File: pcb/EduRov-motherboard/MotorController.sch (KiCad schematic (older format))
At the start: 10 parts, among them IC401 L6203, U201 ACS723xLCTR-05AB

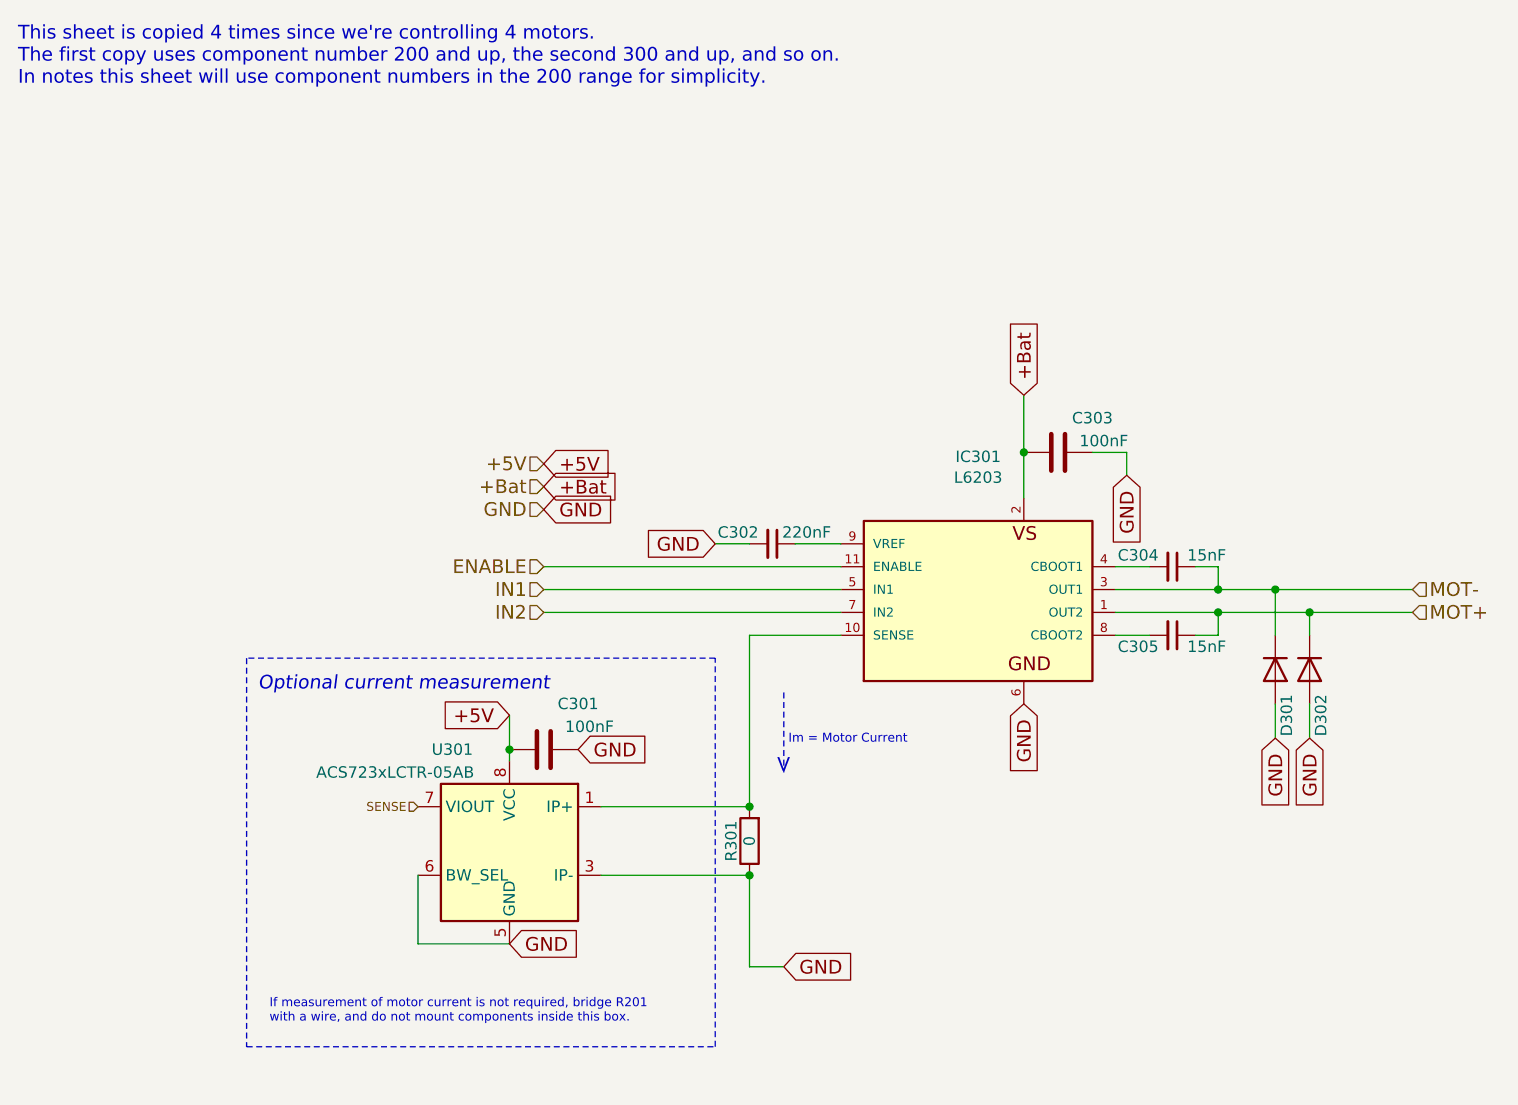
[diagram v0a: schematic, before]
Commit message: Update footprints with models
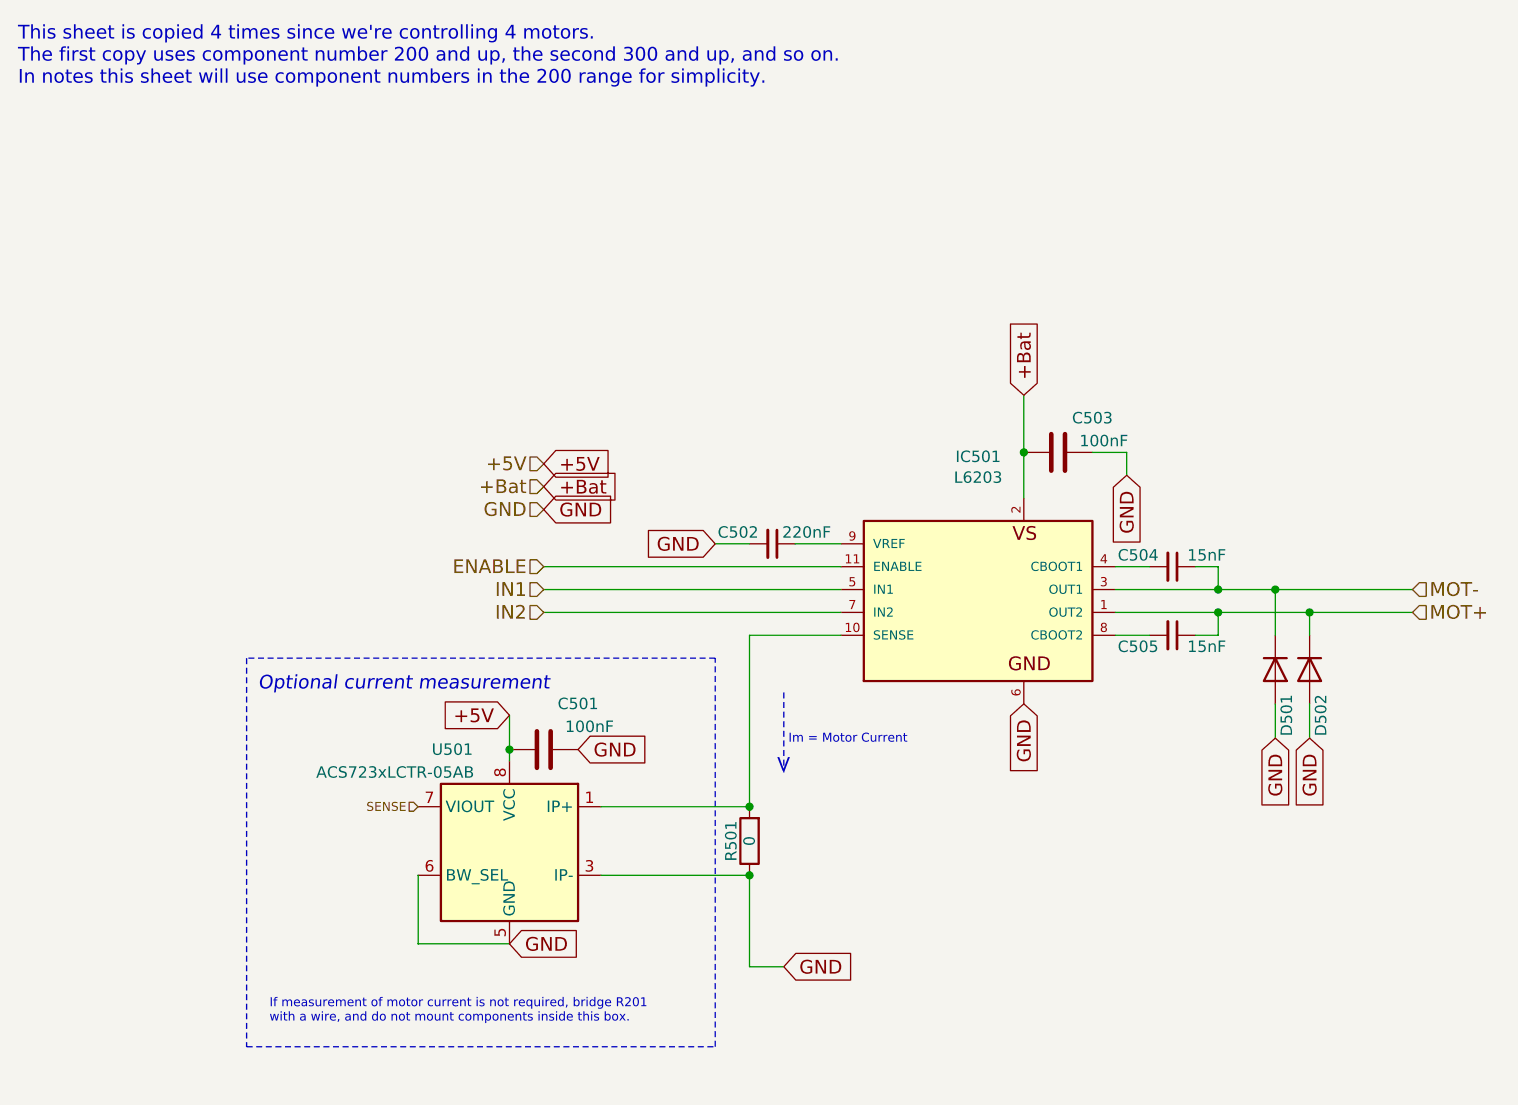
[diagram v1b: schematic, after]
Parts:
- IC401: footprint SnapEDA Library:MULTIWATT-11 -> EduRov:MULTIWATT-11
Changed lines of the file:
@@
 $Descr A4 11693 8268
 encoding utf-8
-Sheet 3 5
+Sheet 5 5
 Title ""
 Date ""
@@
 AR Path="/6003F027/5FFEEEFF" Ref="D402"  Part="1"
 AR Path="/60043462/5FFEEEFF" Ref="D502"  Part="1"
-F 0 "D302" H 6450 3500 50  0000 C CNN
+F 0 "D502" H 6450 3500 50  0000 C CNN
 F 1 "D" H 6400 3400 50  0001 C CNN
 F 2 "Diode_THT:D_DO-41_SOD81_P3.81mm_Vertical_KathodeUp" H 6250 3450 50  0001 C CNN
@@
 AR Path="/6003F027/5FFEEF0B" Ref="D401"  Part="1"
 AR Path="/60043462/5FFEEF0B" Ref="D501"  Part="1"
-F 0 "D301" H 6300 3500 50  0000 C CNN
+F 0 "D501" H 6300 3500 50  0000 C CNN
 F 1 "D" H 6250 3400 50  0001 C CNN
 F 2 "Diode_THT:D_DO-41_SOD81_P3.81mm_Vertical_KathodeUp" H 6100 3450 50  0001 C CNN
@@
 AR Path="/6003F027/5FFEEF49" Ref="C404"  Part="1"
 AR Path="/60043462/5FFEEF49" Ref="C504"  Part="1"
-F 0 "C304" V 5600 2850 50  0000 C CNN
+F 0 "C504" V 5600 2850 50  0000 C CNN
 F 1 "15nF" V 5600 3150 50  0000 C CNN
 F 2 "Capacitor_THT:C_Disc_D3.8mm_W2.6mm_P2.50mm" H 5650 3000 50  0001 C CNN
@@
 AR Path="/6003F027/5FFEEF54" Ref="C405"  Part="1"
 AR Path="/60043462/5FFEEF54" Ref="C505"  Part="1"
-F 0 "C305" V 5700 3150 50  0000 C CNN
+F 0 "C505" V 5700 3150 50  0000 C CNN
 F 1 "15nF" V 5700 3450 50  0000 C CNN
 F 2 "Capacitor_THT:C_Disc_D3.8mm_W2.6mm_P2.50mm" H 5650 3300 50  0001 C CNN
@@
 AR Path="/6003F027/5FFEEF6B" Ref="C402"  Part="1"
 AR Path="/60043462/5FFEEF6B" Ref="C502"  Part="1"
-F 0 "C302" V 3850 2750 50  0000 C CNN
+F 0 "C502" V 3850 2750 50  0000 C CNN
 F 1 "220nF" V 3850 3050 50  0000 C CNN
 F 2 "Capacitor_THT:C_Disc_D3.8mm_W2.6mm_P2.50mm" H 3900 2900 50  0001 C CNN
@@
 AR Path="/6003A868/600F7A3C" Ref="C303"  Part="1"
 AR Path="/6003F027/600F7A3C" Ref="C403"  Part="1"
-F 0 "C303" V 5300 2650 50  0000 C CNN
+F 0 "C503" V 5300 2650 50  0000 C CNN
 F 1 "100nF" V 5200 2700 50  0000 C CNN
 F 2 "Capacitor_THT:C_Disc_D5.0mm_W2.5mm_P2.50mm" H 5188 2350 50  0001 C CNN
@@
 AR Path="/6003F027/6032BA93" Ref="R401"  Part="1"
 AR Path="/60043462/6032BA93" Ref="R501"  Part="1"
-F 0 "R301" V 3880 4200 50  0000 C CNN
+F 0 "R501" V 3880 4200 50  0000 C CNN
 F 1 "0" V 3800 4200 50  0000 C CNN
 F 2 "Resistor_THT:R_Axial_DIN0204_L3.6mm_D1.6mm_P1.90mm_Vertical" V 3730 4200 50  0001 C CNN
@@
 AR Path="/6003F027/60485F83" Ref="U401"  Part="1"
 AR Path="/60043462/60485F83" Ref="U501"  Part="1"
-F 0 "U301" H 3000 4700 50  0000 C CNN
+F 0 "U501" H 3000 4700 50  0000 C CNN
 F 1 "ACS723xLCTR-05AB" H 3250 4600 50  0000 C CNN
 F 2 "Package_SO:SOIC-8_3.9x4.9mm_P1.27mm" H 2850 3900 50  0001 L CIN
@@
 AR Path="/6003A868/60487676" Ref="C301"  Part="1"
 AR Path="/6003F027/60487676" Ref="C401"  Part="1"
-F 0 "C301" V 3100 3950 50  0000 C CNN
+F 0 "C501" V 3100 3950 50  0000 C CNN
 F 1 "100nF" V 3000 4000 50  0000 C CNN
 F 2 "Capacitor_THT:C_Disc_D5.0mm_W2.5mm_P2.50mm" H 2938 3650 50  0001 C CNN
@@
 AR Path="/6003A868/60738BFF" Ref="IC301"  Part="1"
 AR Path="/60043462/60738BFF" Ref="IC501"  Part="1"
-F 0 "IC301" H 4800 3681 50  0000 C CNN
+F 0 "IC501" H 4800 3681 50  0000 C CNN
 F 1 "L6203" H 4800 3590 50  0000 C CNN
-F 2 "SnapEDA Library:MULTIWATT-11" H 4800 3100 50  0001 L BNN
+F 2 "EduRov:MULTIWATT-11" H 4800 3100 50  0001 L BNN
 F 3 "" H 4800 3100 50  0001 L BNN
 F 4 "" H 4800 3100 50  0001 L BNN "MF"

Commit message: Update BOM
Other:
- note added: "If the allegro part is hard to find, \nTMCS1101A4BQDR is a drop-in replacement."
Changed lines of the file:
@@
 $Descr A4 11693 8268
 encoding utf-8
-Sheet 5 5
+Sheet 2 5
 Title ""
 Date ""
@@
 AR Path="/6003F027/5FFEEEFF" Ref="D402"  Part="1"
 AR Path="/60043462/5FFEEEFF" Ref="D502"  Part="1"
-F 0 "D502" H 6450 3500 50  0000 C CNN
+F 0 "D202" H 6450 3500 50  0000 C CNN
 F 1 "D" H 6400 3400 50  0001 C CNN
 F 2 "Diode_THT:D_DO-41_SOD81_P3.81mm_Vertical_KathodeUp" H 6250 3450 50  0001 C CNN
@@
 AR Path="/6003F027/5FFEEF0B" Ref="D401"  Part="1"
 AR Path="/60043462/5FFEEF0B" Ref="D501"  Part="1"
-F 0 "D501" H 6300 3500 50  0000 C CNN
+F 0 "D201" H 6300 3500 50  0000 C CNN
 F 1 "D" H 6250 3400 50  0001 C CNN
 F 2 "Diode_THT:D_DO-41_SOD81_P3.81mm_Vertical_KathodeUp" H 6100 3450 50  0001 C CNN
@@
 AR Path="/6003F027/5FFEEF49" Ref="C404"  Part="1"
 AR Path="/60043462/5FFEEF49" Ref="C504"  Part="1"
-F 0 "C504" V 5600 2850 50  0000 C CNN
+F 0 "C204" V 5600 2850 50  0000 C CNN
 F 1 "15nF" V 5600 3150 50  0000 C CNN
 F 2 "Capacitor_THT:C_Disc_D3.8mm_W2.6mm_P2.50mm" H 5650 3000 50  0001 C CNN
@@
 AR Path="/6003F027/5FFEEF54" Ref="C405"  Part="1"
 AR Path="/60043462/5FFEEF54" Ref="C505"  Part="1"
-F 0 "C505" V 5700 3150 50  0000 C CNN
+F 0 "C205" V 5700 3150 50  0000 C CNN
 F 1 "15nF" V 5700 3450 50  0000 C CNN
 F 2 "Capacitor_THT:C_Disc_D3.8mm_W2.6mm_P2.50mm" H 5650 3300 50  0001 C CNN
@@
 AR Path="/6003F027/5FFEEF6B" Ref="C402"  Part="1"
 AR Path="/60043462/5FFEEF6B" Ref="C502"  Part="1"
-F 0 "C502" V 3850 2750 50  0000 C CNN
+F 0 "C202" V 3850 2750 50  0000 C CNN
 F 1 "220nF" V 3850 3050 50  0000 C CNN
 F 2 "Capacitor_THT:C_Disc_D3.8mm_W2.6mm_P2.50mm" H 3900 2900 50  0001 C CNN
@@
 AR Path="/6003A868/600F7A3C" Ref="C303"  Part="1"
 AR Path="/6003F027/600F7A3C" Ref="C403"  Part="1"
-F 0 "C503" V 5300 2650 50  0000 C CNN
+F 0 "C203" V 5300 2650 50  0000 C CNN
 F 1 "100nF" V 5200 2700 50  0000 C CNN
 F 2 "Capacitor_THT:C_Disc_D5.0mm_W2.5mm_P2.50mm" H 5188 2350 50  0001 C CNN
@@
 AR Path="/6003F027/6032BA93" Ref="R401"  Part="1"
 AR Path="/60043462/6032BA93" Ref="R501"  Part="1"
-F 0 "R501" V 3880 4200 50  0000 C CNN
+F 0 "R201" V 3880 4200 50  0000 C CNN
 F 1 "0" V 3800 4200 50  0000 C CNN
 F 2 "Resistor_THT:R_Axial_DIN0204_L3.6mm_D1.6mm_P1.90mm_Vertical" V 3730 4200 50  0001 C CNN
@@
 AR Path="/6003F027/60485F83" Ref="U401"  Part="1"
 AR Path="/60043462/60485F83" Ref="U501"  Part="1"
-F 0 "U501" H 3000 4700 50  0000 C CNN
+F 0 "U201" H 3000 4700 50  0000 C CNN
 F 1 "ACS723xLCTR-05AB" H 3250 4600 50  0000 C CNN
 F 2 "Package_SO:SOIC-8_3.9x4.9mm_P1.27mm" H 2850 3900 50  0001 L CIN
@@
 AR Path="/6003A868/60487676" Ref="C301"  Part="1"
 AR Path="/6003F027/60487676" Ref="C401"  Part="1"
-F 0 "C501" V 3100 3950 50  0000 C CNN
+F 0 "C201" V 3100 3950 50  0000 C CNN
 F 1 "100nF" V 3000 4000 50  0000 C CNN
 F 2 "Capacitor_THT:C_Disc_D5.0mm_W2.5mm_P2.50mm" H 2938 3650 50  0001 C CNN
@@
 SENSE
 Wire Notes Line
-	1600 3400 1600 5100
-Wire Notes Line
-	1600 5100 3650 5100
-Wire Notes Line
-	3650 5100 3650 3400
+	1600 5275 3650 5275
 $Comp
 L Edurov:L6203 IC401
@@
 AR Path="/6003A868/60738BFF" Ref="IC301"  Part="1"
 AR Path="/60043462/60738BFF" Ref="IC501"  Part="1"
-F 0 "IC501" H 4800 3681 50  0000 C CNN
+F 0 "IC201" H 4800 3681 50  0000 C CNN
 F 1 "L6203" H 4800 3590 50  0000 C CNN
 F 2 "EduRov:MULTIWATT-11" H 4800 3100 50  0001 L BNN
@@
 	1    0    0    -1
 $EndComp
+Text Notes 1700 5175 0    39   ~ 0
+If the allegro part is hard to find, \nTMCS1101A4BQDR is a drop-in replacement.
+Wire Notes Line
+	3650 3400 3650 5275
+Wire Notes Line
+	1600 3400 1600 5275
 $EndSCHEMATC

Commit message: Motherboard updates
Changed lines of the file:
@@
 $Descr A4 11693 8268
 encoding utf-8
-Sheet 2 5
+Sheet 3 5
 Title ""
 Date ""
@@
 AR Path="/6003F027/5FFEEEFF" Ref="D402"  Part="1"
 AR Path="/60043462/5FFEEEFF" Ref="D502"  Part="1"
-F 0 "D202" H 6450 3500 50  0000 C CNN
+F 0 "D302" H 6450 3500 50  0000 C CNN
 F 1 "D" H 6400 3400 50  0001 C CNN
 F 2 "Diode_THT:D_DO-41_SOD81_P3.81mm_Vertical_KathodeUp" H 6250 3450 50  0001 C CNN
@@
 AR Path="/6003F027/5FFEEF0B" Ref="D401"  Part="1"
 AR Path="/60043462/5FFEEF0B" Ref="D501"  Part="1"
-F 0 "D201" H 6300 3500 50  0000 C CNN
+F 0 "D301" H 6300 3500 50  0000 C CNN
 F 1 "D" H 6250 3400 50  0001 C CNN
 F 2 "Diode_THT:D_DO-41_SOD81_P3.81mm_Vertical_KathodeUp" H 6100 3450 50  0001 C CNN
@@
 AR Path="/6003F027/5FFEEF49" Ref="C404"  Part="1"
 AR Path="/60043462/5FFEEF49" Ref="C504"  Part="1"
-F 0 "C204" V 5600 2850 50  0000 C CNN
+F 0 "C304" V 5600 2850 50  0000 C CNN
 F 1 "15nF" V 5600 3150 50  0000 C CNN
 F 2 "Capacitor_THT:C_Disc_D3.8mm_W2.6mm_P2.50mm" H 5650 3000 50  0001 C CNN
@@
 AR Path="/6003F027/5FFEEF54" Ref="C405"  Part="1"
 AR Path="/60043462/5FFEEF54" Ref="C505"  Part="1"
-F 0 "C205" V 5700 3150 50  0000 C CNN
+F 0 "C305" V 5700 3150 50  0000 C CNN
 F 1 "15nF" V 5700 3450 50  0000 C CNN
 F 2 "Capacitor_THT:C_Disc_D3.8mm_W2.6mm_P2.50mm" H 5650 3300 50  0001 C CNN
@@
 AR Path="/6003F027/5FFEEF6B" Ref="C402"  Part="1"
 AR Path="/60043462/5FFEEF6B" Ref="C502"  Part="1"
-F 0 "C202" V 3850 2750 50  0000 C CNN
+F 0 "C302" V 3850 2750 50  0000 C CNN
 F 1 "220nF" V 3850 3050 50  0000 C CNN
 F 2 "Capacitor_THT:C_Disc_D3.8mm_W2.6mm_P2.50mm" H 3900 2900 50  0001 C CNN
@@
 AR Path="/6003A868/600F7A3C" Ref="C303"  Part="1"
 AR Path="/6003F027/600F7A3C" Ref="C403"  Part="1"
-F 0 "C203" V 5300 2650 50  0000 C CNN
+F 0 "C303" V 5300 2650 50  0000 C CNN
 F 1 "100nF" V 5200 2700 50  0000 C CNN
 F 2 "Capacitor_THT:C_Disc_D5.0mm_W2.5mm_P2.50mm" H 5188 2350 50  0001 C CNN
@@
 AR Path="/6003F027/6032BA93" Ref="R401"  Part="1"
 AR Path="/60043462/6032BA93" Ref="R501"  Part="1"
-F 0 "R201" V 3880 4200 50  0000 C CNN
+F 0 "R301" V 3880 4200 50  0000 C CNN
 F 1 "0" V 3800 4200 50  0000 C CNN
 F 2 "Resistor_THT:R_Axial_DIN0204_L3.6mm_D1.6mm_P1.90mm_Vertical" V 3730 4200 50  0001 C CNN
@@
 AR Path="/6003F027/60485F83" Ref="U401"  Part="1"
 AR Path="/60043462/60485F83" Ref="U501"  Part="1"
-F 0 "U201" H 3000 4700 50  0000 C CNN
+F 0 "U301" H 3000 4700 50  0000 C CNN
 F 1 "ACS723xLCTR-05AB" H 3250 4600 50  0000 C CNN
 F 2 "Package_SO:SOIC-8_3.9x4.9mm_P1.27mm" H 2850 3900 50  0001 L CIN
@@
 AR Path="/6003A868/60487676" Ref="C301"  Part="1"
 AR Path="/6003F027/60487676" Ref="C401"  Part="1"
-F 0 "C201" V 3100 3950 50  0000 C CNN
+F 0 "C301" V 3100 3950 50  0000 C CNN
 F 1 "100nF" V 3000 4000 50  0000 C CNN
 F 2 "Capacitor_THT:C_Disc_D5.0mm_W2.5mm_P2.50mm" H 2938 3650 50  0001 C CNN
@@
 AR Path="/6003A868/60738BFF" Ref="IC301"  Part="1"
 AR Path="/60043462/60738BFF" Ref="IC501"  Part="1"
-F 0 "IC201" H 4800 3681 50  0000 C CNN
+F 0 "IC301" H 4800 3681 50  0000 C CNN
 F 1 "L6203" H 4800 3590 50  0000 C CNN
 F 2 "EduRov:MULTIWATT-11" H 4800 3100 50  0001 L BNN
